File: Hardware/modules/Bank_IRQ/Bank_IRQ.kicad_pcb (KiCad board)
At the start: 4 copper layers, 83.3 x 68.2 mm, 33 parts, among them J1 Ports, J2 Bus_PCI_6502, U1 74HC00, U2 74HC138, U3 6525

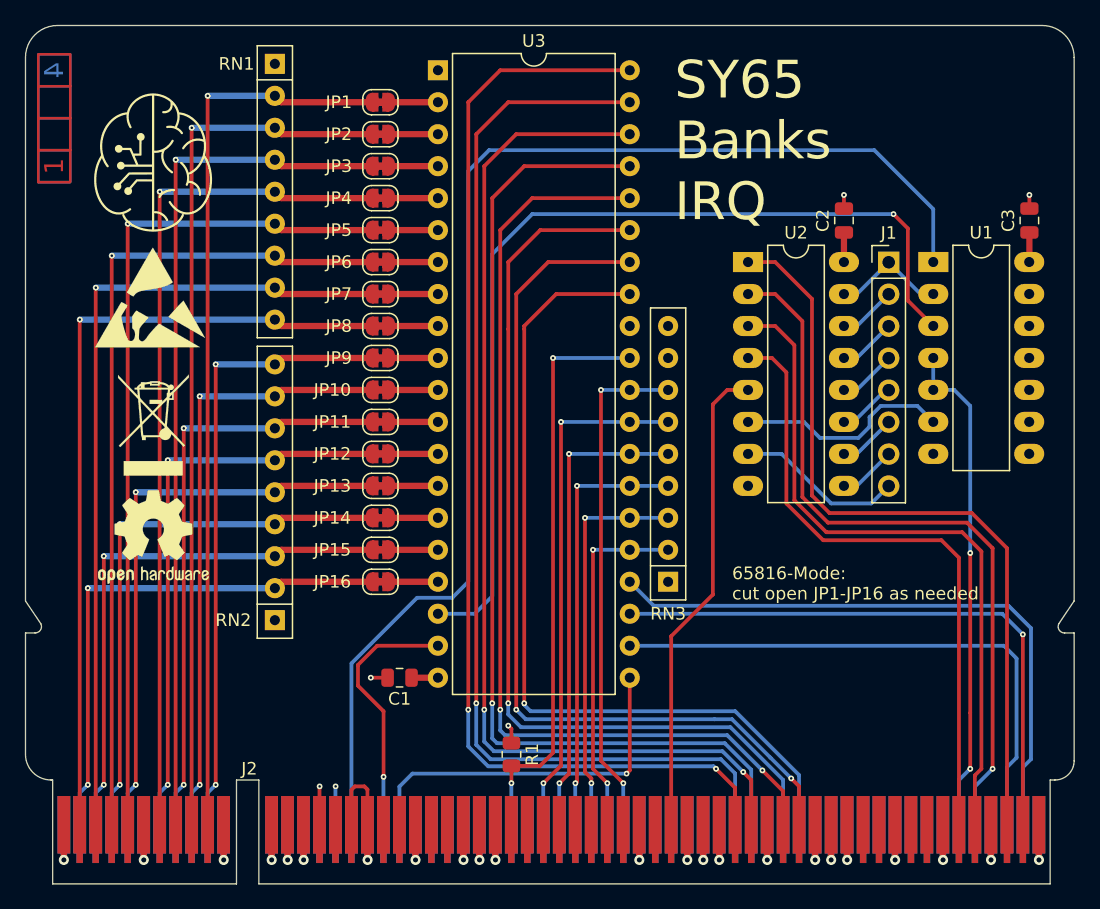
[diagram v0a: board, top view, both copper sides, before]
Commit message: update Silkscreen Bank/IRQ Card
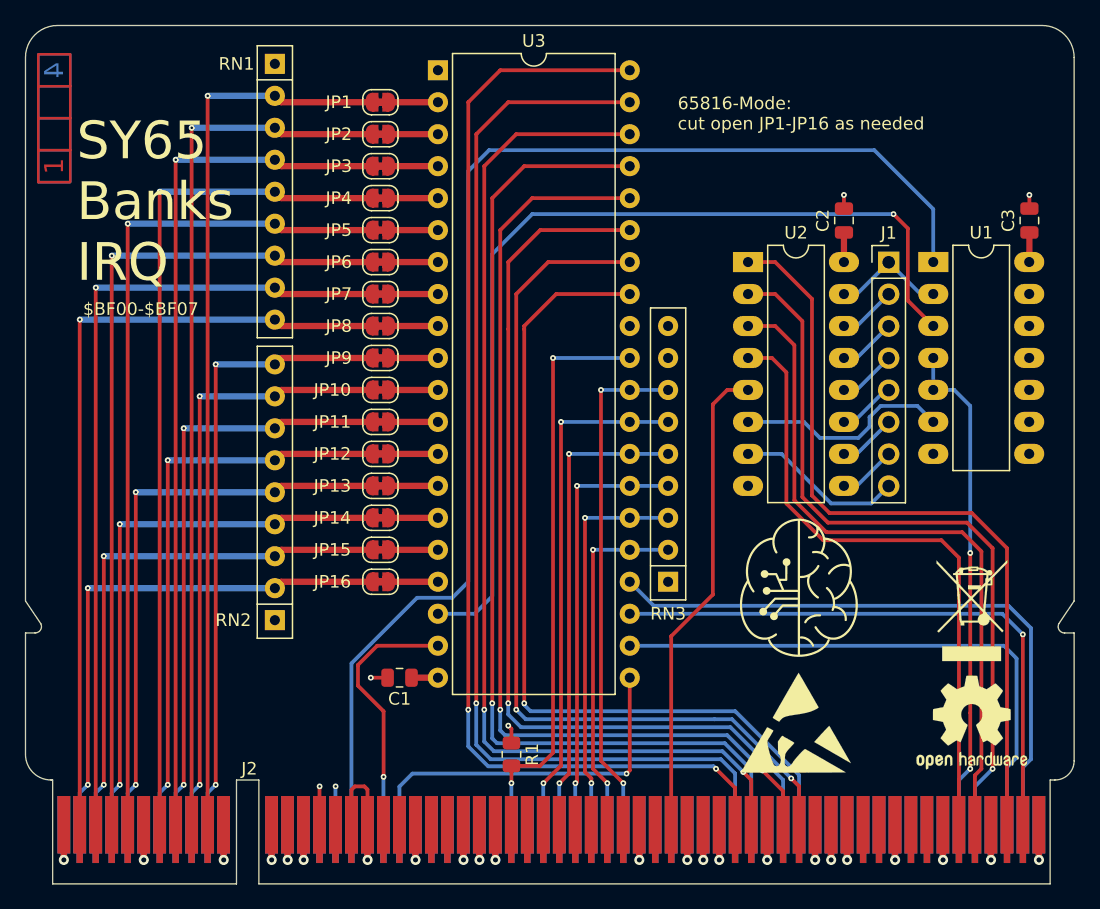
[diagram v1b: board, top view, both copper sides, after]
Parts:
- moved REF** 66.7 mm to (174.8, 114.3)
- moved REF** 66.7 mm to (174.8, 105.4)
- moved G*** 61.4 mm to (161.0, 103.6)
- moved REF** 61.4 mm to (160.8, 114.3)
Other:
- board text added: "$BF00-$BF07"
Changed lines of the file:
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@@
 	(footprint "Symbol:OSHW-Logo2_9.8x8mm_SilkScreen"
 		(layer "F.Cu")
-		(at 109.728 99.568)
+		(at 174.752 114.3)
 		(descr "Open Source Hardware Symbol")
 		(tags "Logo Symbol OSHW")
@@
 	(footprint "Symbol:WEEE-Logo_5.6x8mm_SilkScreen"
 		(layer "F.Cu")
-		(at 109.728 90.678)
+		(at 174.752 105.41)
 		(descr "Waste Electrical and Electronic Equipment Directive")
 		(tags "Logo WEEE")
@@
 	(footprint "Symbol:ESD-Logo_8.9x8mm_SilkScreen"
 		(layer "F.Cu")
-		(at 109.474 80.518)
+		(at 160.782 114.3)
 		(descr "Electrostatic discharge Logo")
 		(tags "Logo ESD")
@@
 	(footprint "Eigene:logo"
 		(layer "F.Cu")
-		(at 109.728 69.85)
+		(at 161.036 103.632)
 		(property "Reference" "G***"
 			(at 0 0 0)
@@
 		(tags "PCI bus Edge Connector")
 		(property "Reference" "J2"
-			(at 23.998 5.78 -180)
+			(at 23.998 5.78 180)
 			(layer "F.SilkS")
 			(effects
@@
 	)
 	(gr_text "SY65\nBanks\nIRQ"
-		(at 151.13 74.676 0)
+		(at 103.632 79.502 0)
 		(layer "F.SilkS")
 		(effects
@@
 		)
 	)
+	(gr_text "$BF00-$BF07"
+		(at 104.14 82.042 0)
+		(layer "F.SilkS")
+		(effects
+			(font
+				(size 1 1)
+				(thickness 0.15)
+			)
+			(justify left bottom)
+		)
+	)
 	(gr_text "65816-Mode:\ncut open JP1-JP16 as needed"
-		(at 155.702 104.648 0)
+		(at 151.384 67.31 0)
 		(layer "F.SilkS")
 		(effects

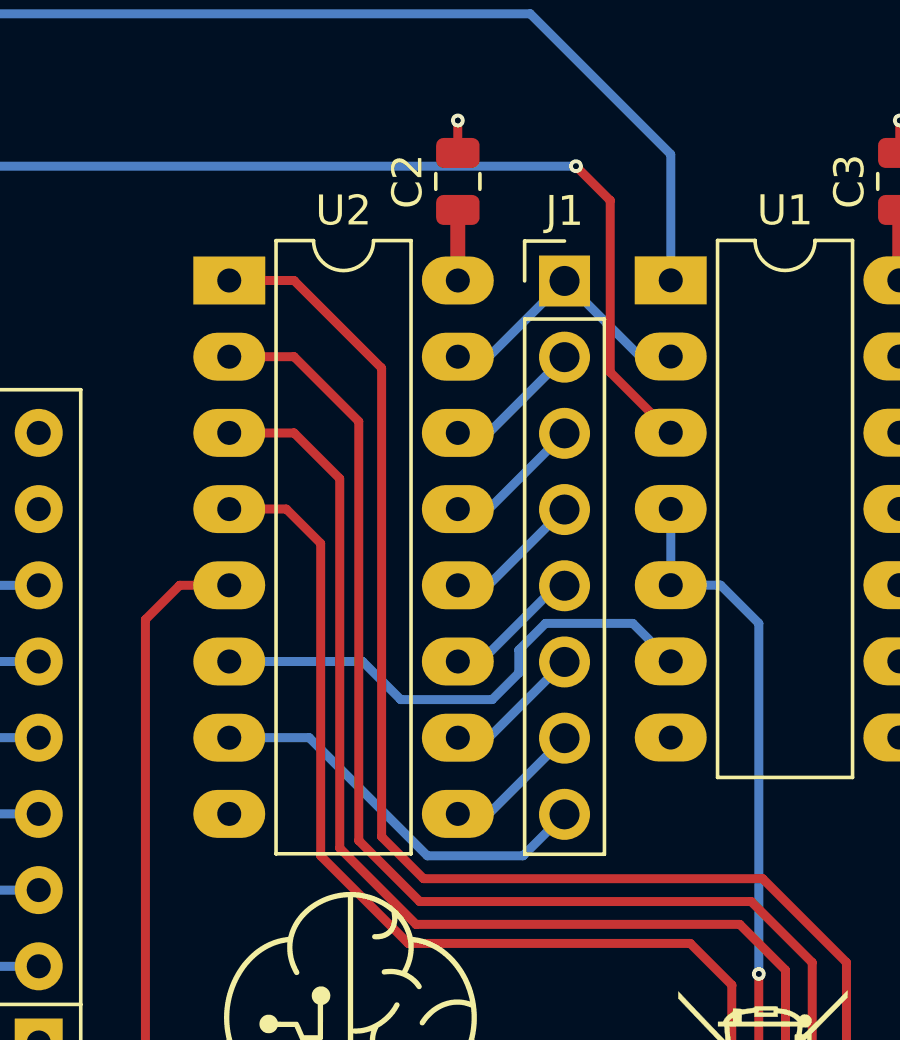
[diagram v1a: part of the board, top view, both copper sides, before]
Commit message: Hardware Update Add MyCPU VGA Module Beautify all Schematics minor Error corrections Readme Update
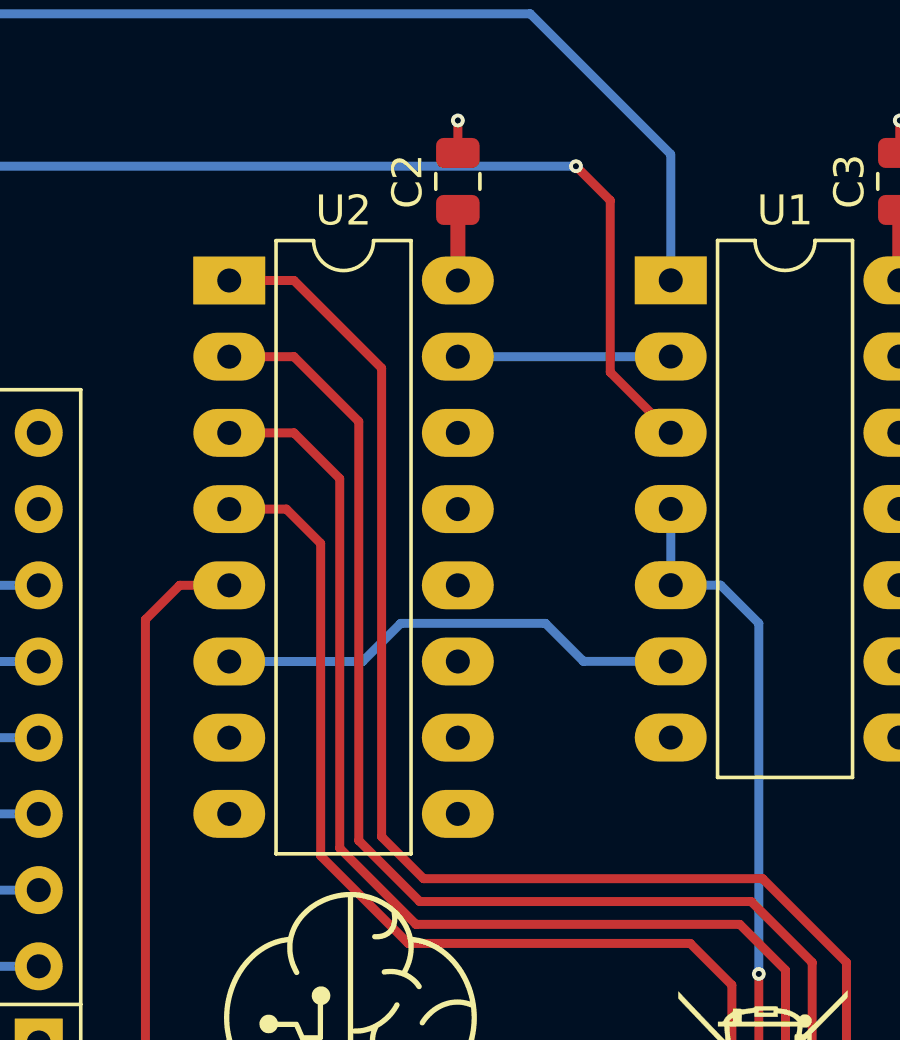
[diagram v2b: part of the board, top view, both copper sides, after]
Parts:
- removed J1: Ports, Connector_PinHeader_2.54mm:PinHeader_1x08_P2.54mm_Vertical
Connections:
- J2 pad A11: /A13 -> unconnected-(J2-A13-PadA11)
- J2 pad A12: /A15 -> unconnected-(J2-A15-PadA12)
- J2 pad A25: /~{ROM} -> unconnected-(J2-~{ROM}-PadA25)
- J2 pad A27: /~{IRQ_0.0} -> unconnected-(J2-~{IRQ_0.0}-PadA27)_0
- J2 pad A28: /~{IRQ_0.1} -> unconnected-(J2-~{IRQ_0.1}-PadA28)
- J2 pad A29: /~{IRQ_0.2} -> unconnected-(J2-~{IRQ_0.2}-PadA29)_0
- J2 pad A30: /~{IRQ_0.3} -> unconnected-(J2-~{IRQ_0.3}-PadA30)
- J2 pad A31: /~{IRQ_0.4} -> unconnected-(J2-~{IRQ_0.4}-PadA31)_0
- J2 pad A32: /~{IRQ_0.5} -> unconnected-(J2-~{IRQ_0.5}-PadA32)_0
- J2 pad A33: /~{IRQ_0.6} -> unconnected-(J2-~{IRQ_0.6}-PadA33)_0
- J2 pad A34: /~{IRQ_0.7} -> unconnected-(J2-~{IRQ_0.7}-PadA34)_0
- J2 pad A38: /SYNC_VPA -> unconnected-(J2-Sync/VPA-PadA38)_0
- J2 pad A39: /Ø2/VDA -> unconnected-(J2-Ø2/VDA-PadA39)_0
- J2 pad A41: /~{RDY} -> unconnected-(J2-~{RDY}-PadA41)_0
- J2 pad A42: /~{BE} -> unconnected-(J2-~{BE}-PadA42)
- J2 pad A45: /E -> unconnected-(J2-E-PadA45)_0
- J2 pad A8: /A9 -> unconnected-(J2-A9-PadA8)_0
- J2 pad A9: /A11 -> unconnected-(J2-A11-PadA9)_0
- J2 pad B11: /A12 -> unconnected-(J2-A12-PadB11)_0
- J2 pad B12: /A14 -> unconnected-(J2-A14-PadB12)
- J2 pad B24: /~{L_RAM} -> unconnected-(J2-~{L_RAM}-PadB24)
- J2 pad B25: /~{H_RAM} -> unconnected-(J2-~{H_RAM}-PadB25)
- J2 pad B33: /~{NMI} -> unconnected-(J2-~{NMI}-PadB33)_0
- J2 pad B38: /~{VP} -> unconnected-(J2-~{VP}-PadB38)
- J2 pad B39: /~{ML} -> unconnected-(J2-~{ML}-PadB39)
- J2 pad B46: /M/X -> unconnected-(J2-M/~{X}-PadB46)_0
- J2 pad B8: /A8 -> unconnected-(J2-A8-PadB8)
- J2 pad B9: /A10 -> unconnected-(J2-A10-PadB9)
- U2 pad 10: /PORT_40 -> unconnected-(U2-~{Y5}-Pad10)
- U2 pad 11: /PORT_32 -> unconnected-(U2-~{Y4}-Pad11)
- U2 pad 12: /PORT_24 -> unconnected-(U2-~{Y3}-Pad12)
- U2 pad 13: /PORT_16 -> unconnected-(U2-~{Y2}-Pad13)
- U2 pad 14: /PORT_8 -> unconnected-(U2-~{Y1}-Pad14)
- U2 pad 7: /PORT_56 -> unconnected-(U2-~{Y7}-Pad7)
- U2 pad 9: /PORT_48 -> unconnected-(U2-~{Y6}-Pad9)
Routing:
- net /PORT_56: track 13.4 -> 0.00 mm
- net /PORT_32: track 4.60 -> 0.00 mm
- net /PORT_8: track 4.60 -> 0.00 mm
- net /PORT_48: track 4.60 -> 0.00 mm
- net /PORT_40: track 4.60 -> 0.00 mm
- net /PORT_24: track 4.60 -> 0.00 mm
- net /PORT_16: track 4.60 -> 0.00 mm
- net /PORT_0: track 9.19 -> 7.11 mm
- net Net-(U2-E2): track 17.3 -> 15.8 mm
- net unconnected-(U2-~{Y6}-Pad9): track 0.00 -> 1.03 mm
- net unconnected-(U2-~{Y5}-Pad10): track 0.00 -> 1.03 mm
- net unconnected-(U2-~{Y2}-Pad13): track 0.00 -> 1.03 mm
- net unconnected-(U2-~{Y1}-Pad14): track 0.00 -> 1.03 mm
- net unconnected-(U2-~{Y3}-Pad12): track 0.00 -> 1.02 mm
- net unconnected-(U2-~{Y4}-Pad11): track 0.00 -> 0.76 mm

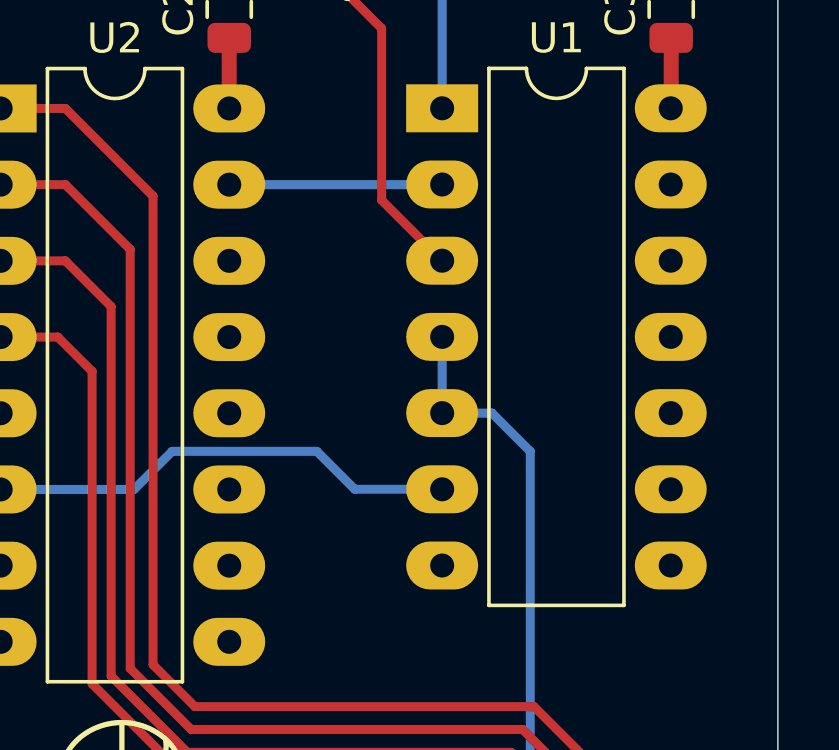
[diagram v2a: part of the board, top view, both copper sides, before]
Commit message: Chip Select Strobe Generation Bugfix
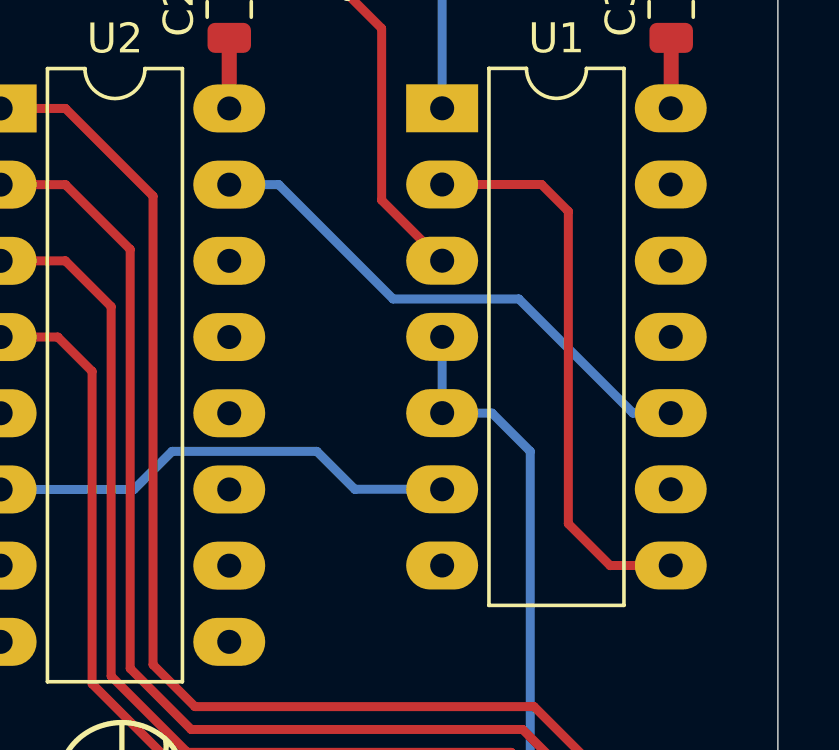
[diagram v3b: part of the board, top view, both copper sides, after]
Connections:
- U1 pad 10: GND -> Net-(U2-~{Y0})
- U1 pad 8: unconnected-(U1-Pad8) -> /PORT_0
- U1 pad 9: GND -> Net-(U2-~{Y0})
- U2 pad 15: /PORT_0 -> Net-(U2-~{Y0})
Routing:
- net Net-(U2-~{Y0}): track 0.00 -> 17.9 mm
- net /PORT_0: track 7.11 -> 20.0 mm
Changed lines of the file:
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@@
 	(net 102 "Net-(U3-~{CS})")
 	(net 103 "unconnected-(U1-Pad11)")
-	(net 104 "unconnected-(U1-Pad8)")
+	(net 104 "Net-(U2-~{Y0})")
 	(net 105 "unconnected-(U3-PC7-Pad32)")
 	(net 106 "unconnected-(J2-A8-PadB8)")
@@
 			(layers "*.Cu" "*.Mask")
 			(remove_unused_layers no)
-			(net 78 "/PORT_0")
+			(net 104 "Net-(U2-~{Y0})")
 			(pinfunction "~{Y0}")
 			(pintype "output")
@@
 			(layers "*.Cu" "*.Mask")
 			(remove_unused_layers no)
-			(net 104 "unconnected-(U1-Pad8)")
-			(pintype "output+no_connect")
+			(net 78 "/PORT_0")
+			(pintype "output")
 		)
 		(pad "9" thru_hole oval
@@
 			(layers "*.Cu" "*.Mask")
 			(remove_unused_layers no)
-			(net 2 "GND")
+			(net 104 "Net-(U2-~{Y0})")
 			(pintype "input")
 		)
@@
 			(layers "*.Cu" "*.Mask")
 			(remove_unused_layers no)
-			(net 2 "GND")
+			(net 104 "Net-(U2-~{Y0})")
 			(pintype "input")
 		)
@@
 	)
 	(segment
-		(start 170.673 80.264)
-		(end 170.668 80.259)
+		(start 175.001 80.259)
+		(end 175.895 81.153)
 		(width 0.3)
-		(layer "B.Cu")
+		(layer "F.Cu")
+		(net 78)
+	)
+	(segment
+		(start 177.292 92.964)
+		(end 177.297 92.959)
+		(width 0.3)
+		(layer "F.Cu")
 		(net 78)
 	)
 	(segment
-		(start 164.592 80.264)
-		(end 170.673 80.264)
+		(start 175.895 91.567)
+		(end 177.292 92.964)
+		(width 0.3)
+		(layer "F.Cu")
+		(net 78)
+	)
+	(segment
+		(start 171.689 80.259)
+		(end 175.001 80.259)
+		(width 0.3)
+		(layer "F.Cu")
+		(net 78)
+	)
+	(segment
+		(start 177.297 92.959)
+		(end 179.309 92.959)
+		(width 0.3)
+		(layer "F.Cu")
+		(net 78)
+	)
+	(segment
+		(start 175.895 81.153)
+		(end 175.895 91.567)
+		(width 0.3)
+		(layer "F.Cu")
+		(net 78)
+	)
+	(segment
+		(start 170.673 80.264)
+		(end 170.668 80.259)
 		(width 0.3)
 		(layer "B.Cu")
@@
 	)
 	(segment
+		(start 174.244 84.074)
+		(end 170.053 84.074)
+		(width 0.3)
+		(layer "B.Cu")
+		(net 104)
+	)
+	(segment
+		(start 178.049 87.879)
+		(end 174.244 84.074)
+		(width 0.3)
+		(layer "B.Cu")
+		(net 104)
+	)
+	(segment
+		(start 179.309 87.879)
+		(end 178.049 87.879)
+		(width 0.3)
+		(layer "B.Cu")
+		(net 104)
+	)
+	(segment
+		(start 166.243 80.264)
+		(end 164.592 80.264)
+		(width 0.3)
+		(layer "B.Cu")
+		(net 104)
+	)
+	(segment
+		(start 170.053 84.074)
+		(end 166.243 80.264)
+		(width 0.3)
+		(layer "B.Cu")
+		(net 104)
+	)
+	(segment

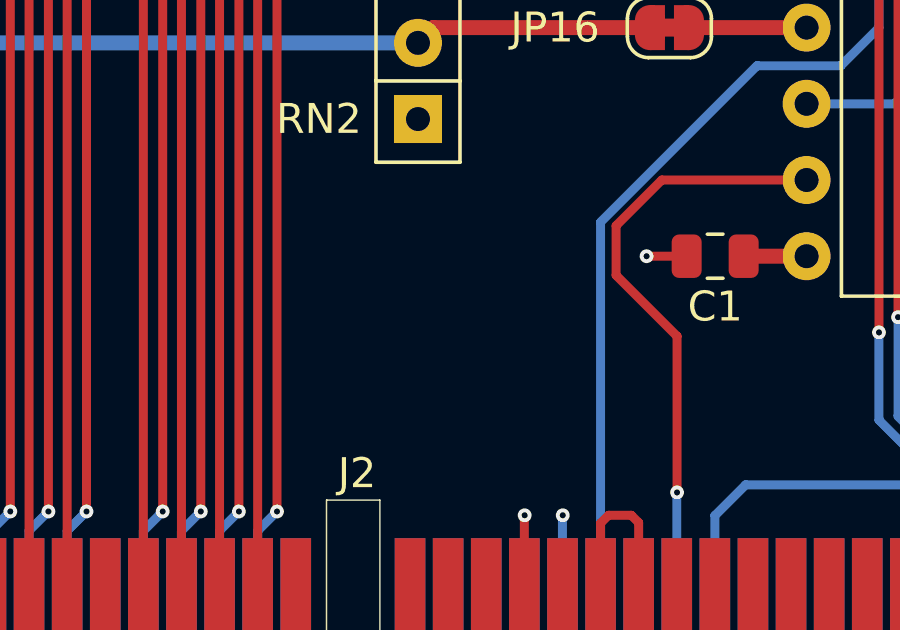
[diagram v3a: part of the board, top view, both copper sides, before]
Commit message: Hardware Review Pt. 1 fix Address Decoding for Strobe Generators add bulk capacitance to every board fix wiring of Prototyping Board
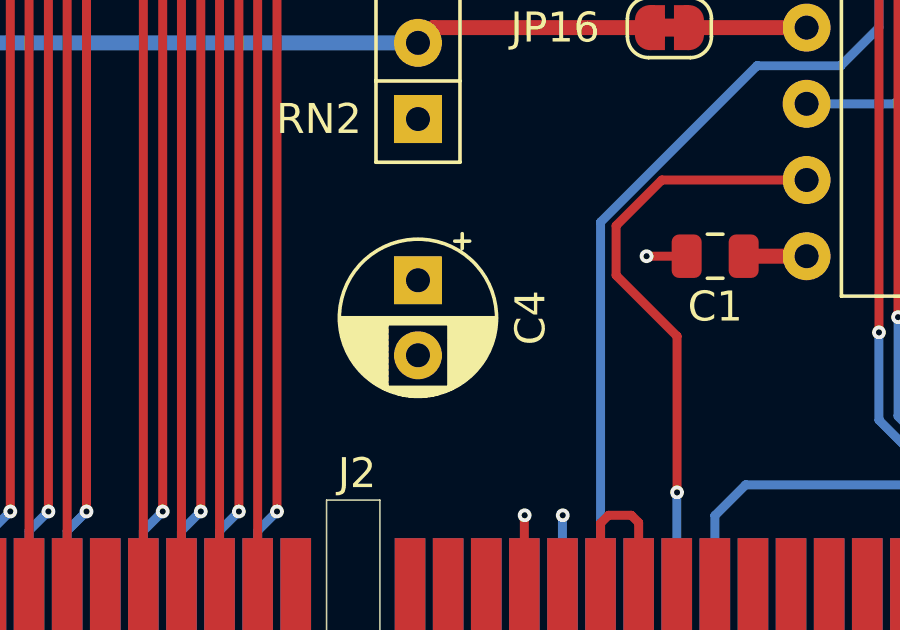
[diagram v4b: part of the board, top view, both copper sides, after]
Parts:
- added C4: 10µ, Capacitor_THT:CP_Radial_D5.0mm_P2.50mm, F.Cu at (119.4, 111.5)
